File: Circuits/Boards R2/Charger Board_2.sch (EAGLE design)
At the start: 65 parts, among them CON1 ISP(2X3), CON10 HEADER_3X1, CON11 HEADER_3X1, CON12 HEADER_3X1, CON2 SCREWTERMINAL_1X2, CON3 HEADER_3X1, CON4 HEADER_3X1, CON5 HEADER_3X1, CON6 HEADER_3X1, CON7 HEADER_3X1, CON8 HEADER_3X1, CON9 HEADER_3X1, IC1 NCP1117DT33G, T1 NPN2N2222, T2 NPN2N2222, T3 SI4421DY, U1 ATMEGA324P, U2 ACS711

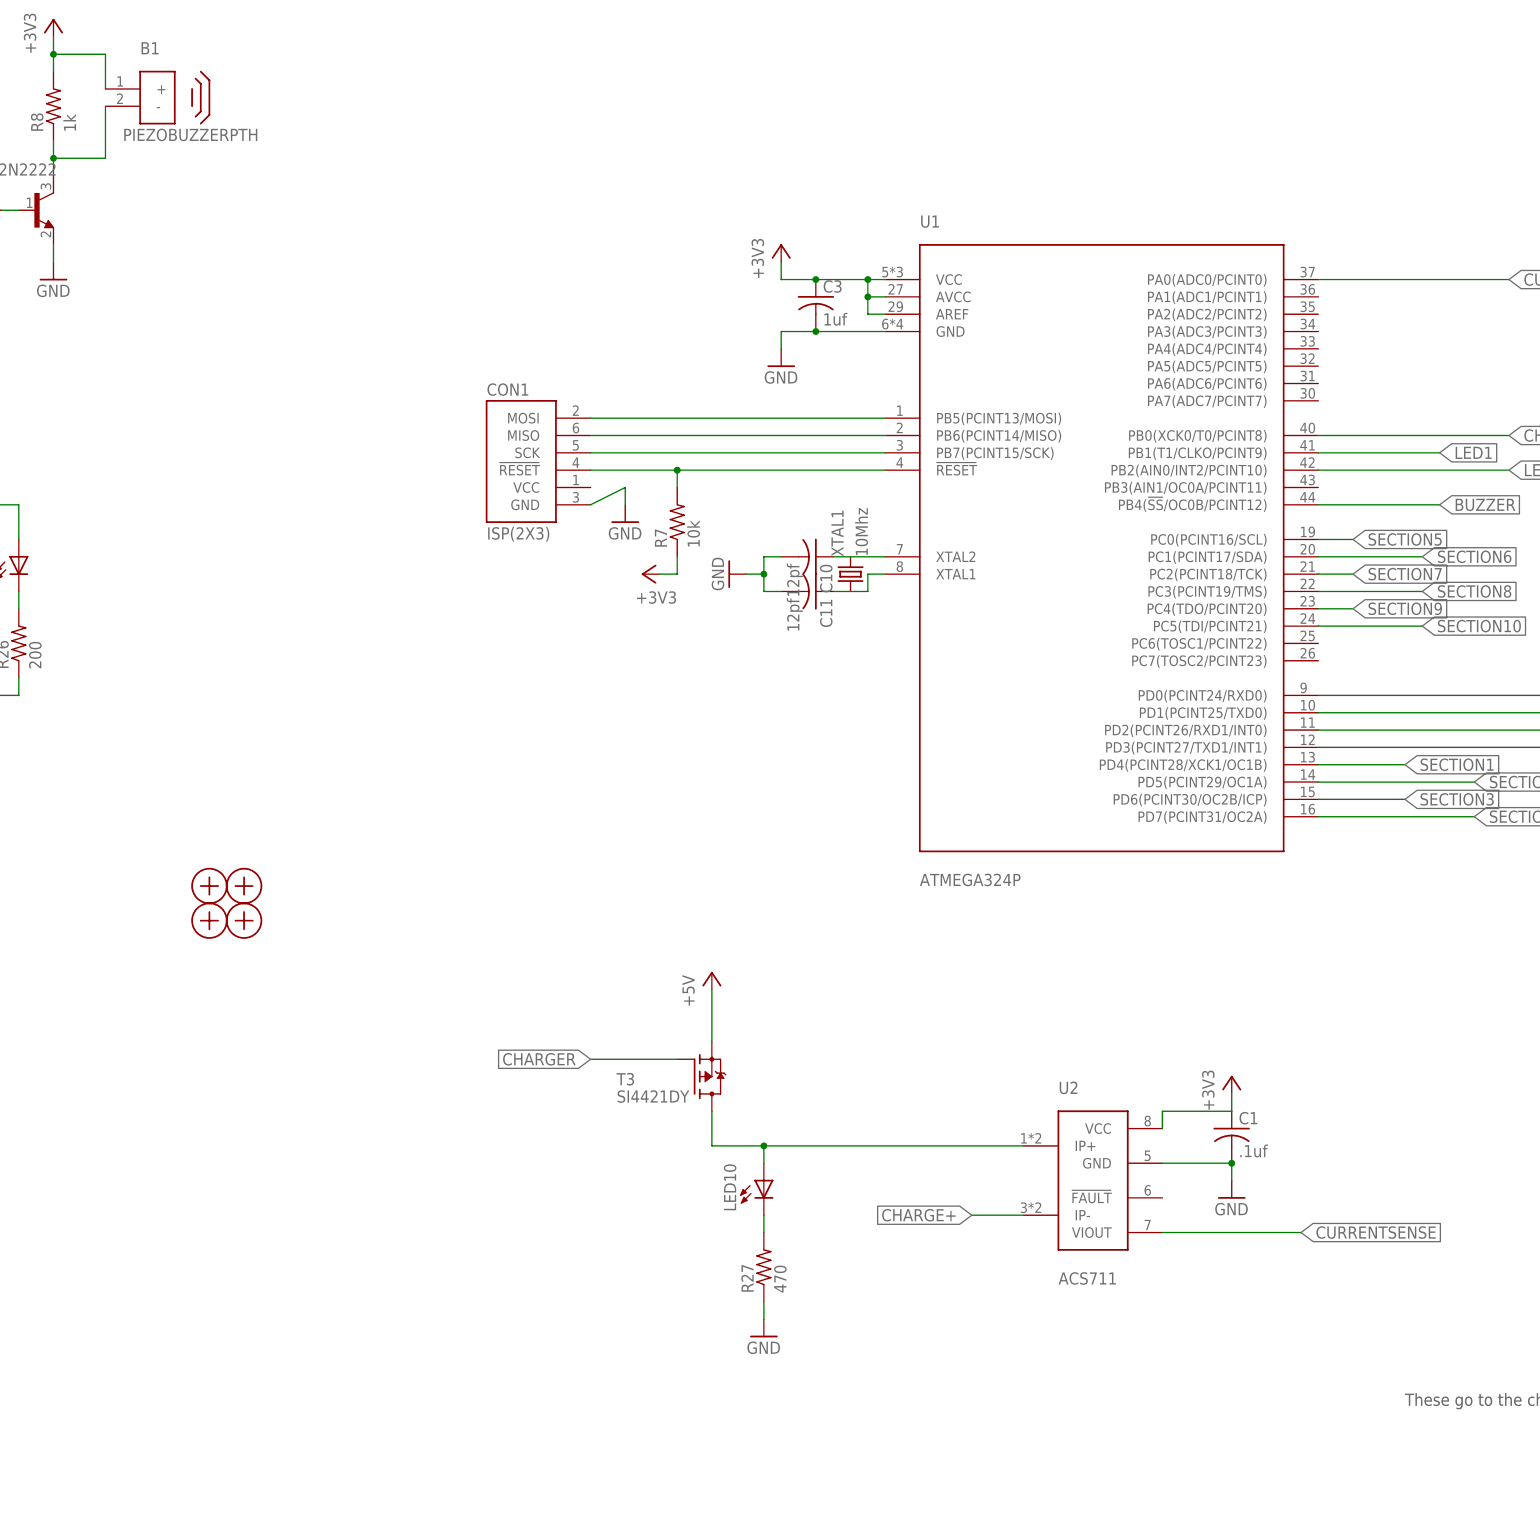
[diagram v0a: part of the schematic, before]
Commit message: updated swarm board with R2 and started charger board changes
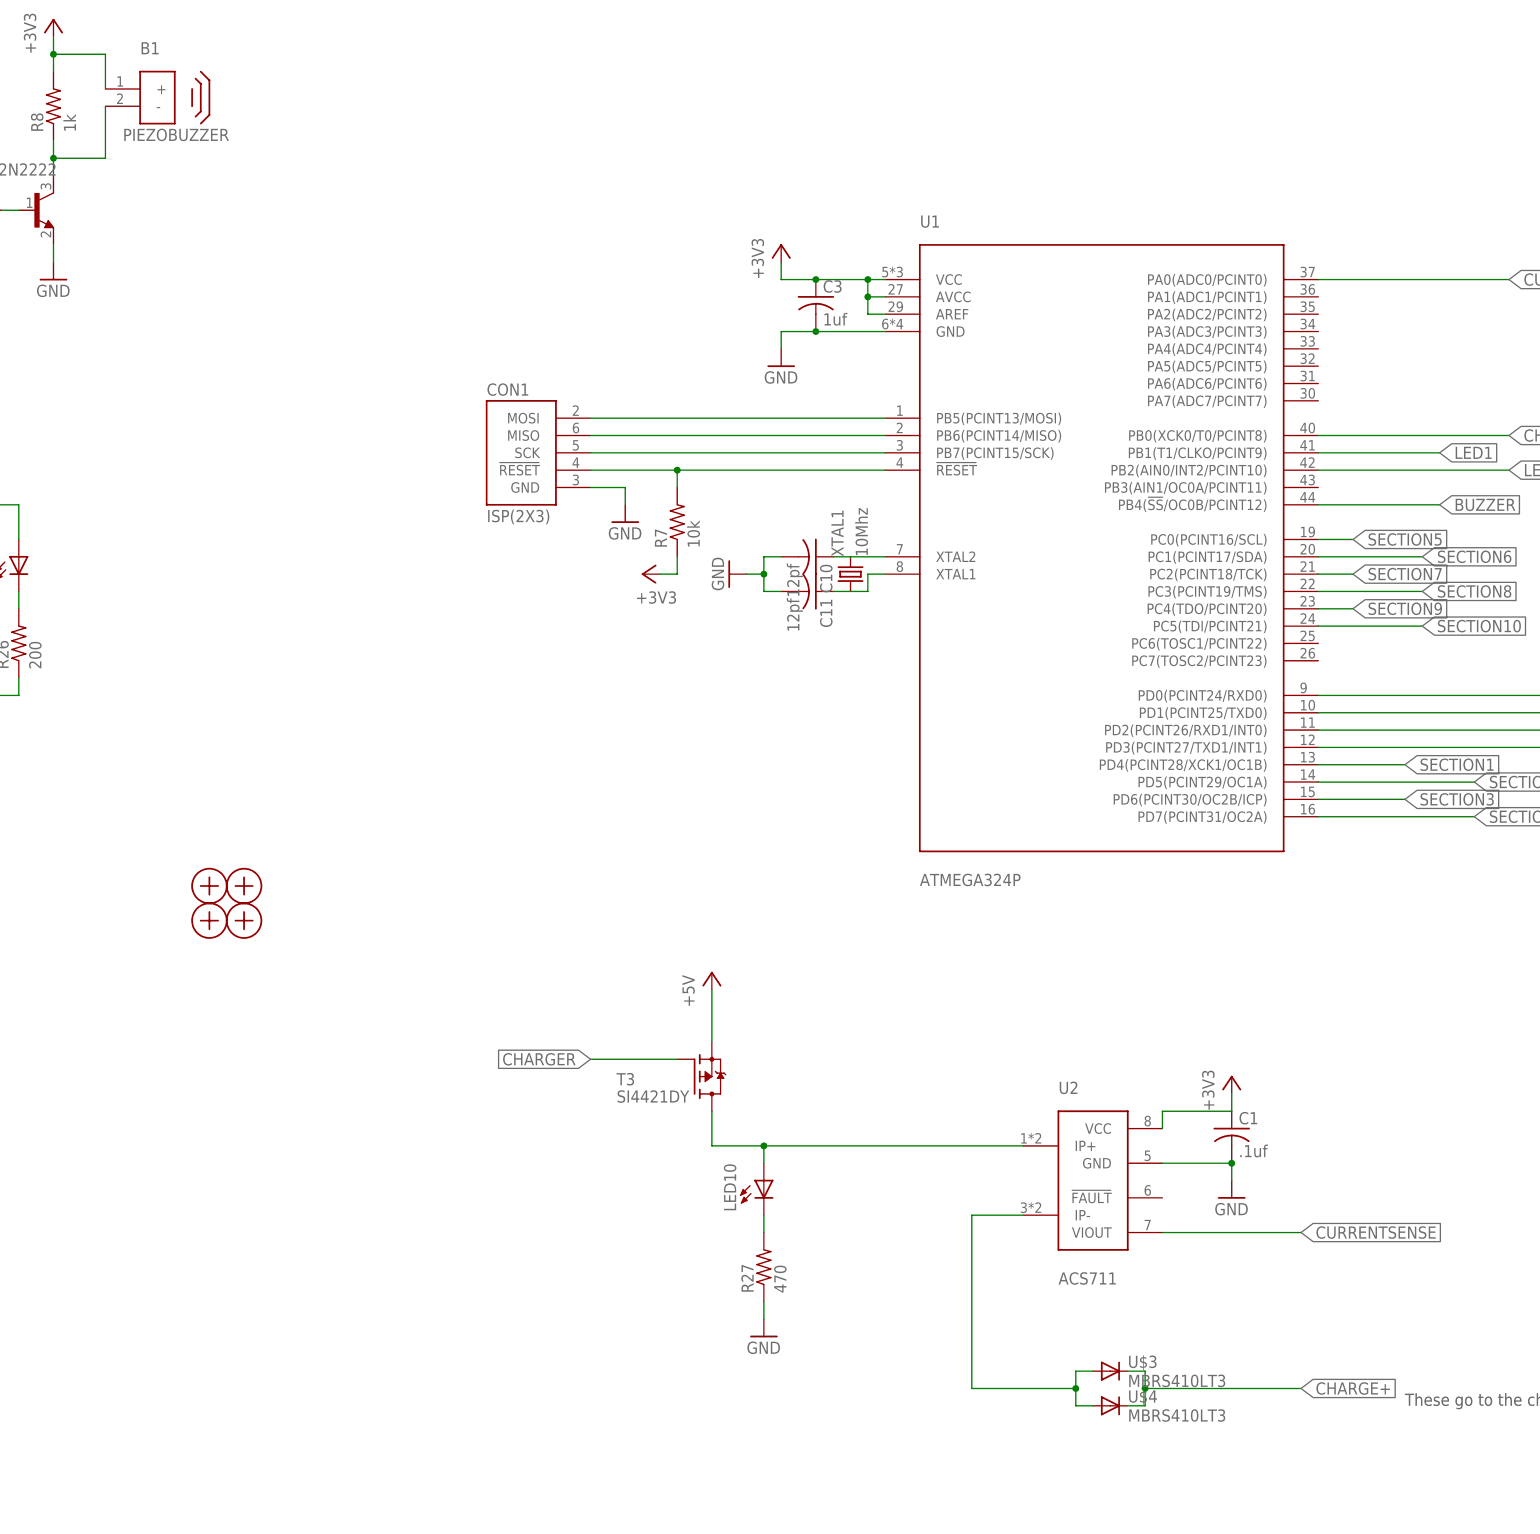
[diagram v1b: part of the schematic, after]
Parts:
- added U$3, U$4: MBRS410LT3, Passive:MBRS410LT3
- B1: value PIEZOBUZZERPTH -> PIEZOBUZZER; device Passive:PIEZOBUZZERPTH -> Passive:PIEZOBUZZER
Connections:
- new net N$23: U$3.A, U$4.A, U2.IP-
- net CHARGE+: now also U$3.C, U$4.C; no longer U2.IP-
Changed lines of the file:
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@@
 <part name="CON1" library="Mechanical" deviceset="ISP" device="(2X3)"/>
 <part name="GND5" library="Supply" deviceset="GND" device=""/>
+<part name="B1" library="Passive" deviceset="PIEZOBUZZER" device=""/>
 <part name="R8" library="Passive" deviceset="RES" device="0603" value="1k"/>
 <part name="GND6" library="Supply" deviceset="GND" device=""/>
@@
 <part name="R19" library="Passive" deviceset="RES" device="0603" value="100"/>
 <part name="R20" library="Passive" deviceset="RES" device="0603" value="100"/>
+<part name="U$3" library="Passive" deviceset="MBRS410LT3" device=""/>
+<part name="U$4" library="Passive" deviceset="MBRS410LT3" device=""/>
 <part name="XTAL1" library="Passive" deviceset="NX5032GA-10.000000MHZ" device="" value="10Mhz"/>
 <part name="C10" library="Passive" deviceset="CAP" device="0603" value="12pf"/>
@@
 <part name="CON2" library="Mechanical" deviceset="SCREWTERMINAL_1X2" device=""/>
 <part name="GND12" library="Supply" deviceset="GND" device=""/>
-<part name="B1" library="Passive" deviceset="PIEZOBUZZER" device="PTH"/>
 </parts>
 <sheets>
@@
 <instance part="CON1" gate="G$1" x="-86.36" y="12.7"/>
 <instance part="GND5" gate="1" x="147.32" y="-30.48"/>
+<instance part="B1" gate="G$1" x="-142.24" y="63.5"/>
 <instance part="R8" gate="G$1" x="-154.94" y="63.5" rot="R90"/>
 <instance part="GND6" gate="1" x="-154.94" y="38.1"/>
@@
 <instance part="R19" gate="G$1" x="358.14" y="-114.3" rot="R90"/>
 <instance part="R20" gate="G$1" x="381" y="-114.3" rot="R90"/>
+<instance part="U$3" gate="G$1" x="0" y="-121.92"/>
+<instance part="U$4" gate="G$1" x="0" y="-127"/>
 <instance part="XTAL1" gate="G$1" x="-38.1" y="-5.08" rot="R90"/>
 <instance part="C10" gate="G$1" x="-45.72" y="-2.54" rot="R270"/>
@@
 <instance part="CON2" gate="G$1" x="-27.94" y="99.06" rot="MR0"/>
 <instance part="GND12" gate="1" x="-20.32" y="88.9"/>
-<instance part="B1" gate="G$1" x="-142.24" y="63.5"/>
 </instances>
 <busses>
@@
 </segment>
 <segment>
-<wire x1="-76.2" y1="5.08" x2="-71.12" y2="7.62" width="0.1524" layer="91"/>
+<wire x1="-76.2" y1="7.62" x2="-71.12" y2="7.62" width="0.1524" layer="91"/>
 <wire x1="-71.12" y1="7.62" x2="-71.12" y2="5.08" width="0.1524" layer="91"/>
 <pinref part="GND4" gate="1" pin="GND"/>
@@
 <net name="N$9" class="0">
 <segment>
+<pinref part="B1" gate="G$1" pin="-"/>
 <wire x1="-147.32" y1="63.5" x2="-147.32" y2="55.88" width="0.1524" layer="91"/>
 <wire x1="-147.32" y1="55.88" x2="-154.94" y2="55.88" width="0.1524" layer="91"/>
@@
 <wire x1="-154.94" y1="55.88" x2="-154.94" y2="53.34" width="0.1524" layer="91"/>
 <pinref part="T1" gate="G$1" pin="C"/>
-<pinref part="B1" gate="G$1" pin="-"/>
 </segment>
 </net>
@@
 </net>
 <net name="CHARGE+" class="0">
+<segment>
+<wire x1="27.94" y1="-124.46" x2="5.08" y2="-124.46" width="0.1524" layer="91"/>
+<wire x1="5.08" y1="-124.46" x2="5.08" y2="-121.92" width="0.1524" layer="91"/>
+<wire x1="5.08" y1="-121.92" x2="2.54" y2="-121.92" width="0.1524" layer="91"/>
+<wire x1="5.08" y1="-124.46" x2="5.08" y2="-127" width="0.1524" layer="91"/>
+<wire x1="5.08" y1="-127" x2="2.54" y2="-127" width="0.1524" layer="91"/>
+<label x="27.94" y="-124.46" size="1.778" layer="91" xref="yes"/>
+<junction x="5.08" y="-124.46"/>
+<pinref part="U$3" gate="G$1" pin="C"/>
+<pinref part="U$4" gate="G$1" pin="C"/>
+</segment>
 <segment>
 <wire x1="154.94" y1="-101.6" x2="172.72" y2="-101.6" width="0.1524" layer="91"/>
@@
 <label x="154.94" y="-101.6" size="1.778" layer="91" rot="R180" xref="yes"/>
 </segment>
-<segment>
+</net>
+<net name="N$23" class="0">
+<segment>
+<wire x1="-2.54" y1="-121.92" x2="-5.08" y2="-121.92" width="0.1524" layer="91"/>
+<wire x1="-2.54" y1="-127" x2="-5.08" y2="-127" width="0.1524" layer="91"/>
+<wire x1="-5.08" y1="-127" x2="-5.08" y2="-124.46" width="0.1524" layer="91"/>
 <pinref part="U2" gate="G$1" pin="IP-"/>
+<wire x1="-5.08" y1="-124.46" x2="-5.08" y2="-121.92" width="0.1524" layer="91"/>
 <wire x1="-12.7" y1="-99.06" x2="-20.32" y2="-99.06" width="0.1524" layer="91"/>
-<label x="-20.32" y="-99.06" size="1.778" layer="91" rot="R180" xref="yes"/>
+<wire x1="-20.32" y1="-99.06" x2="-20.32" y2="-124.46" width="0.1524" layer="91"/>
+<wire x1="-5.08" y1="-124.46" x2="-20.32" y2="-124.46" width="0.1524" layer="91"/>
+<junction x="-5.08" y="-124.46"/>
+<pinref part="U$3" gate="G$1" pin="A"/>
+<pinref part="U$4" gate="G$1" pin="A"/>
 </segment>
 </net>
@@
 <pinref part="R8" gate="G$1" pin="2"/>
 <wire x1="-154.94" y1="73.66" x2="-154.94" y2="71.12" width="0.1524" layer="91"/>
+<pinref part="B1" gate="G$1" pin="+"/>
 <wire x1="-154.94" y1="71.12" x2="-154.94" y2="68.58" width="0.1524" layer="91"/>
 <wire x1="-154.94" y1="71.12" x2="-147.32" y2="71.12" width="0.1524" layer="91"/>
@@
 <junction x="-154.94" y="71.12"/>
 <pinref part="+3V5" gate="G$1" pin="+3V3"/>
-<pinref part="B1" gate="G$1" pin="+"/>
-</segment>
-<segment>
+</segment>
+<segment>

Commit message: saving charger changes
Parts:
- removed LED8, LED9: (no value), Passive:LED0603
- removed R25, R26: 200, Passive:RES0603
- added C2, C7: .1uf, Passive:CAP0603
- added LED1: SMD_RGB, Passive:SMD_RGB
- added R1: 310, Passive:RES0603
- added R21, R22: 200, Passive:RES0603
- LED10: value (none) -> red
- R16: value 500 -> 1k
- R28: value (none) -> 1k
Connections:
- removed net N$20: LED8.C, R25.2
- removed net N$21: LED9.C, R26.2
- new net LED3: R1.1, U1.PB3(AIN1/OC0A/PCINT11)
- new net N$37: LED1.REDCATHODE, R1.2
- new net N$38: LED1.BLUECATHODE, R21.2
- new net N$39: LED1.GREENCATHODE, R22.2
- new net SCL: U1.PC0(PCINT16/SCL)
- new net SDA: U1.PC1(PCINT17/SDA)
- net +3V3: now also C2.1, C7.1, CON1.VCC
- net +5V: now also LED1.COMMONANODE
- net GND: now also C2.2, C7.2; no longer R25.1, R26.1
- net LED1: now also R21.1; no longer LED9.A
- net LED2: now also R22.1; no longer LED8.A
- net SECTION10: now also U1.PC7(TOSC2/PCINT23); no longer U1.PC5(TDI/PCINT21)
- net SECTION5: now also U1.PC2(PCINT18/TCK); no longer U1.PC0(PCINT16/SCL)
- net SECTION6: now also U1.PC3(PCINT19/TMS); no longer U1.PC1(PCINT17/SDA)
- net SECTION7: now also U1.PC4(TDO/PCINT20); no longer U1.PC2(PCINT18/TCK)
- net SECTION8: now also U1.PC5(TDI/PCINT21); no longer U1.PC3(PCINT19/TMS)
- net SECTION9: now also U1.PC6(TOSC1/PCINT22); no longer U1.PC4(TDO/PCINT20)
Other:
- moved on the sheet: B1, C6

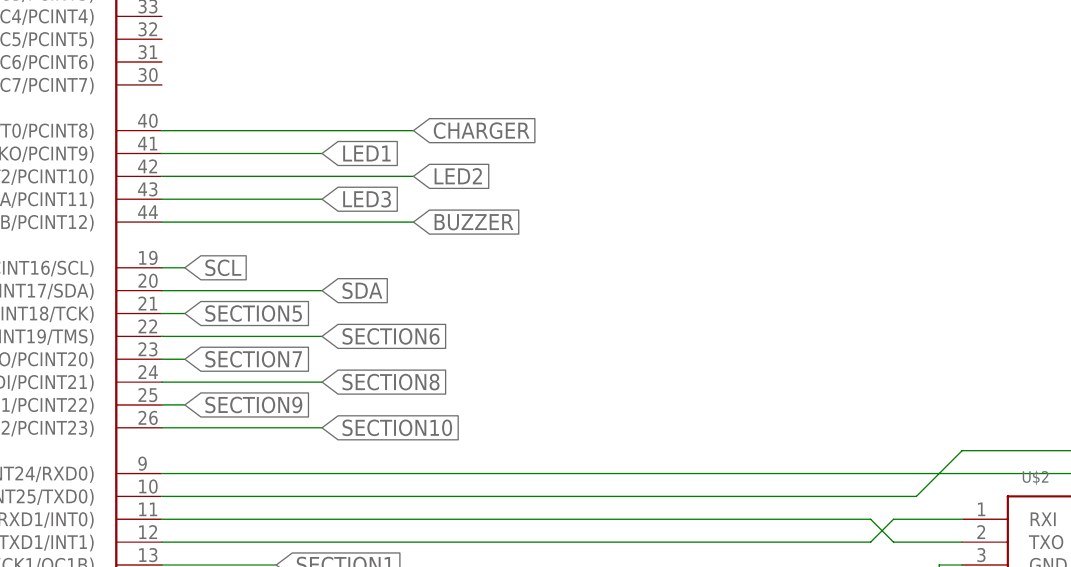
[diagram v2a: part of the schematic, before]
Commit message: 
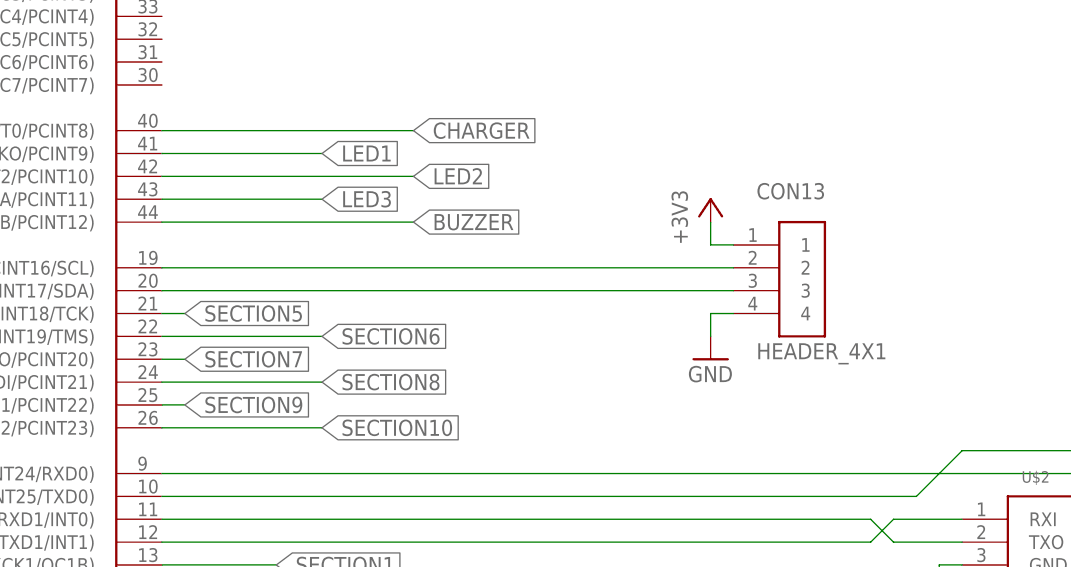
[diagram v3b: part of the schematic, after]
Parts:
- added CON13: HEADER_4X1, Mechanical:HEADER_4X1
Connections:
- net +3V3: now also CON13.1
- net GND: now also CON13.4
- net SCL: now also CON13.2
- net SDA: now also CON13.3
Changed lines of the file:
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@@
 <part name="C2" library="Passive" deviceset="CAP" device="0603" value=".1uf"/>
 <part name="C7" library="Passive" deviceset="CAP" device="0603" value=".1uf"/>
+<part name="CON13" library="Mechanical" deviceset="HEADER_4X1" device=""/>
+<part name="GND11" library="Supply" deviceset="GND" device=""/>
+<part name="+3V8" library="Supply" deviceset="+3V3" device=""/>
 </parts>
 <sheets>
@@
 <instance part="C2" gate="G$1" x="228.6" y="71.12"/>
 <instance part="C7" gate="G$1" x="236.22" y="71.12"/>
+<instance part="CON13" gate="G$1" x="99.06" y="0"/>
+<instance part="GND11" gate="1" x="91.44" y="-10.16"/>
+<instance part="+3V8" gate="G$1" x="91.44" y="7.62"/>
 </instances>
 <busses>
@@
 <pinref part="GND12" gate="1" pin="GND"/>
 </segment>
+<segment>
+<pinref part="CON13" gate="G$1" pin="4"/>
+<wire x1="93.98" y1="-5.08" x2="91.44" y2="-5.08" width="0.1524" layer="91"/>
+<wire x1="91.44" y1="-5.08" x2="91.44" y2="-7.62" width="0.1524" layer="91"/>
+<pinref part="GND11" gate="1" pin="GND"/>
+</segment>
 </net>
 <net name="N$2" class="0">
@@
 <pinref part="+3V4" gate="G$1" pin="+3V3"/>
 </segment>
+<segment>
+<pinref part="CON13" gate="G$1" pin="1"/>
+<wire x1="93.98" y1="2.54" x2="91.44" y2="2.54" width="0.1524" layer="91"/>
+<wire x1="91.44" y1="2.54" x2="91.44" y2="5.08" width="0.1524" layer="91"/>
+<pinref part="+3V8" gate="G$1" pin="+3V3"/>
+</segment>
 </net>
 <net name="SECTION2" class="0">
@@
 <segment>
 <pinref part="U1" gate="G$1" pin="PC0(PCINT16/SCL)"/>
-<wire x1="30.48" y1="0" x2="33.02" y2="0" width="0.1524" layer="91"/>
-<label x="33.02" y="0" size="1.778" layer="91" xref="yes"/>
+<wire x1="30.48" y1="0" x2="93.98" y2="0" width="0.1524" layer="91"/>
+<pinref part="CON13" gate="G$1" pin="2"/>
 </segment>
 </net>
@@
 <segment>
 <pinref part="U1" gate="G$1" pin="PC1(PCINT17/SDA)"/>
-<wire x1="30.48" y1="-2.54" x2="48.26" y2="-2.54" width="0.1524" layer="91"/>
-<label x="48.26" y="-2.54" size="1.778" layer="91" xref="yes"/>
-</segment>
-</net>
+<wire x1="30.48" y1="-2.54" x2="93.98" y2="-2.54" width="0.1524" layer="91"/>
+<pinref part="CON13" gate="G$1" pin="3"/>
+</segment>
+</net>
